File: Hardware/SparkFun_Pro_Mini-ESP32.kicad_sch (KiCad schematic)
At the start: 22 parts, among them J1 Conn_01x06, J2 Conn_01x12, J3 Conn_01x12, J4 Qwiic_RA, SW1 Reset, SW2 Boot, U1 ESP32-PICO-V3-02, U2 AP2112K-3.3

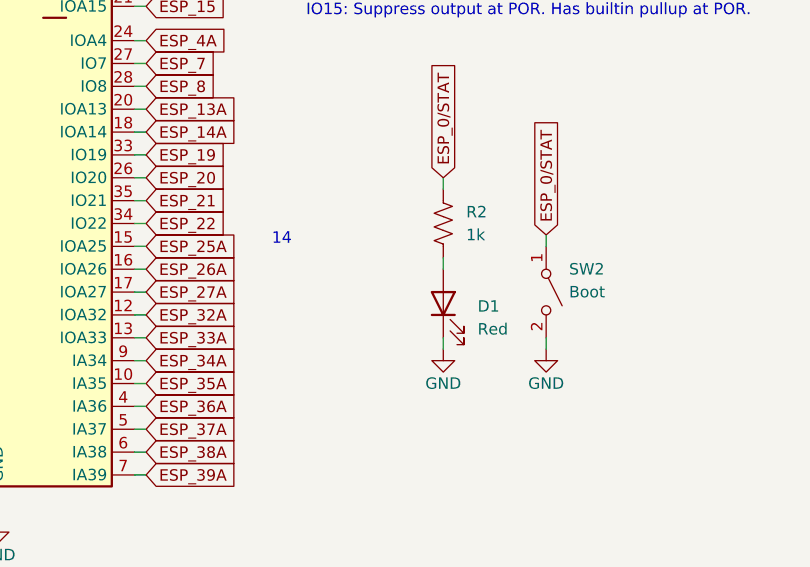
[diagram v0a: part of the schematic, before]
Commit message: Update status LED to green.
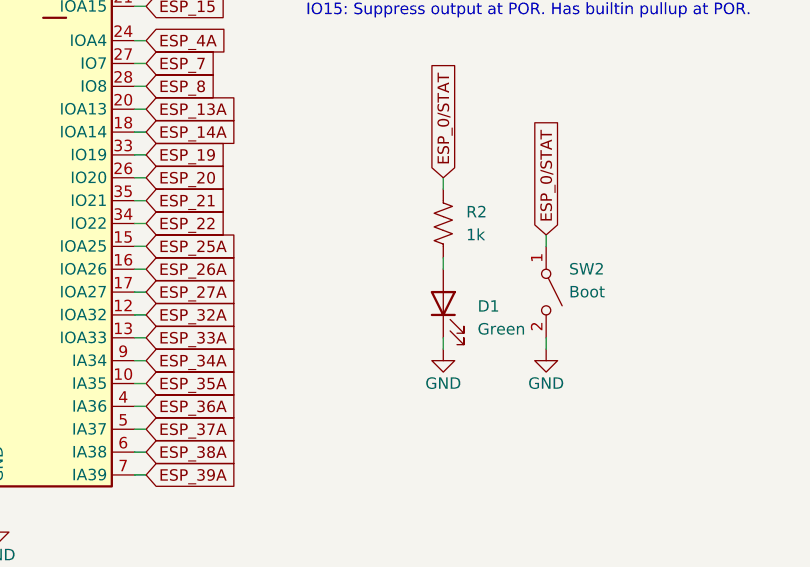
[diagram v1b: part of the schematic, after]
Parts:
- D1: value Red -> Green; symbol SparkFun-LED:LED_Red_0603 -> SparkFun-LED:LED_Green_0603; PROD_ID DIO-00819 -> DIO-00821
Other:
- note removed: "14"
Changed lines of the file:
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@@
-    (effects (font (size 1.27 1.27)) (justify left bottom))
-  )
-  (text "14" (at 91.44 82.55 0)
     (effects (font (size 1.27 1.27)) (justify left bottom))
   )
@@
     )
   )
-  (symbol (lib_id "SparkFun-LED:LED_Red_0603") (at 110.49 88.9 90) (unit 1)
+  (symbol (lib_id "SparkFun-LED:LED_Green_0603") (at 110.49 88.9 90) (unit 1)
     (in_bom yes) (on_board yes) (dnp no) (fields_autoplaced)
     (property "Reference" "D1" (at 114.3 89.2175 90)
       (effects (font (size 1.27 1.27)) (justify right))
     )
-    (property "Value" "Red" (at 114.3 91.7575 90)
+    (property "Value" "Green" (at 114.3 91.7575 90)
       (effects (font (size 1.27 1.27)) (justify right))
     )
-    (property "Footprint" "SparkFun-LED:LED_0603_1608Metric" (at 116.84 88.9 0)
-      (effects (font (size 1.27 1.27)) hide)
-    )
-    (property "Datasheet" "https://docs.broadcom.com/docs/AV02-0551EN" (at 110.49 88.9 0)
-      (effects (font (size 1.27 1.27)) hide)
-    )
-    (property "PROD_ID" "DIO-00819" (at 115.062 88.9 0)
-      (effects (font (size 1.27 1.27)) hide)
-    )
+    (property "Footprint" "SparkFun-LED:LED_0603_1608Metric" (at 115.57 88.9 0)
+      (effects (font (size 1.27 1.27)) hide)
+    )
+    (property "Datasheet" "https://docs.broadcom.com/docs/AV02-0551EN" (at 120.65 88.9 0)
+      (effects (font (size 1.27 1.27)) hide)
+    )
+    (property "PROD_ID" "DIO-00821" (at 118.364 89.154 0)
+      (effects (font (size 1.27 1.27)) hide)
+    )
